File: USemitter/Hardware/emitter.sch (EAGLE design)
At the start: 8 parts, among them U5 LM1117MP-3.3

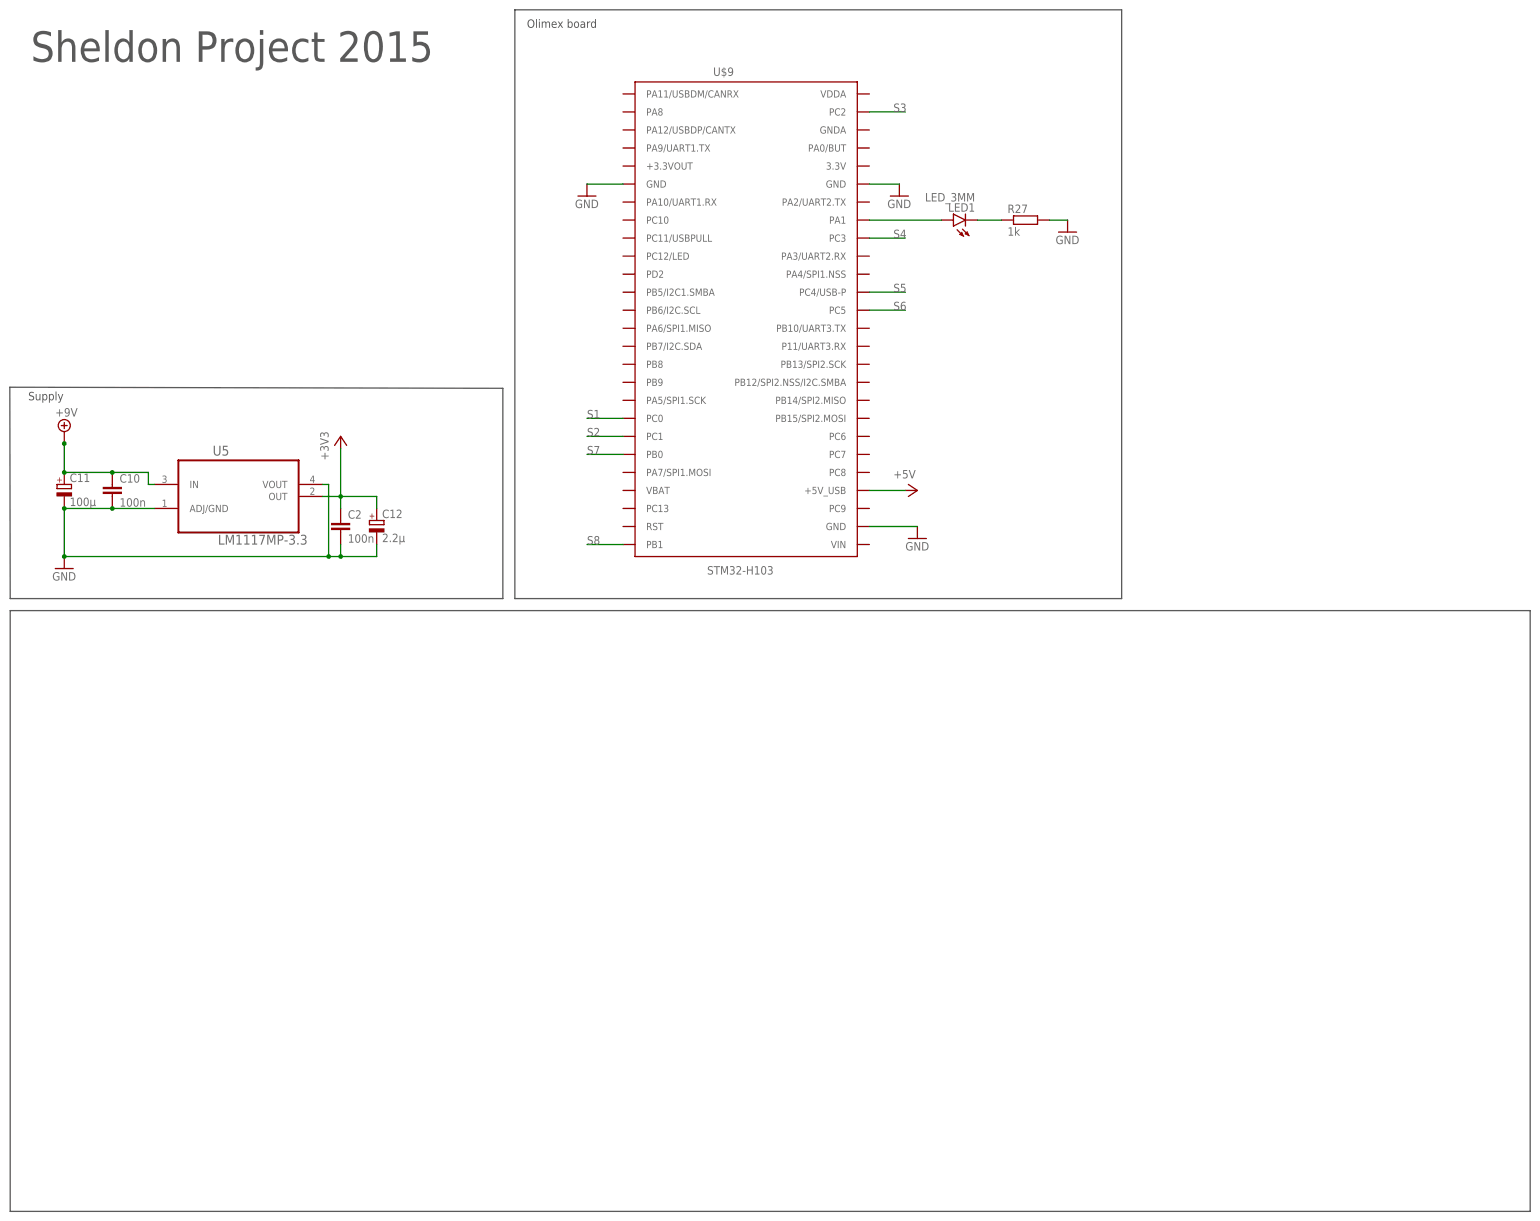
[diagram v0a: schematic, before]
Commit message: - Emitter schematic almost finished. - STM32 code generator modified to integrate the LED and the reversed PWM. ==> Code must still be generated
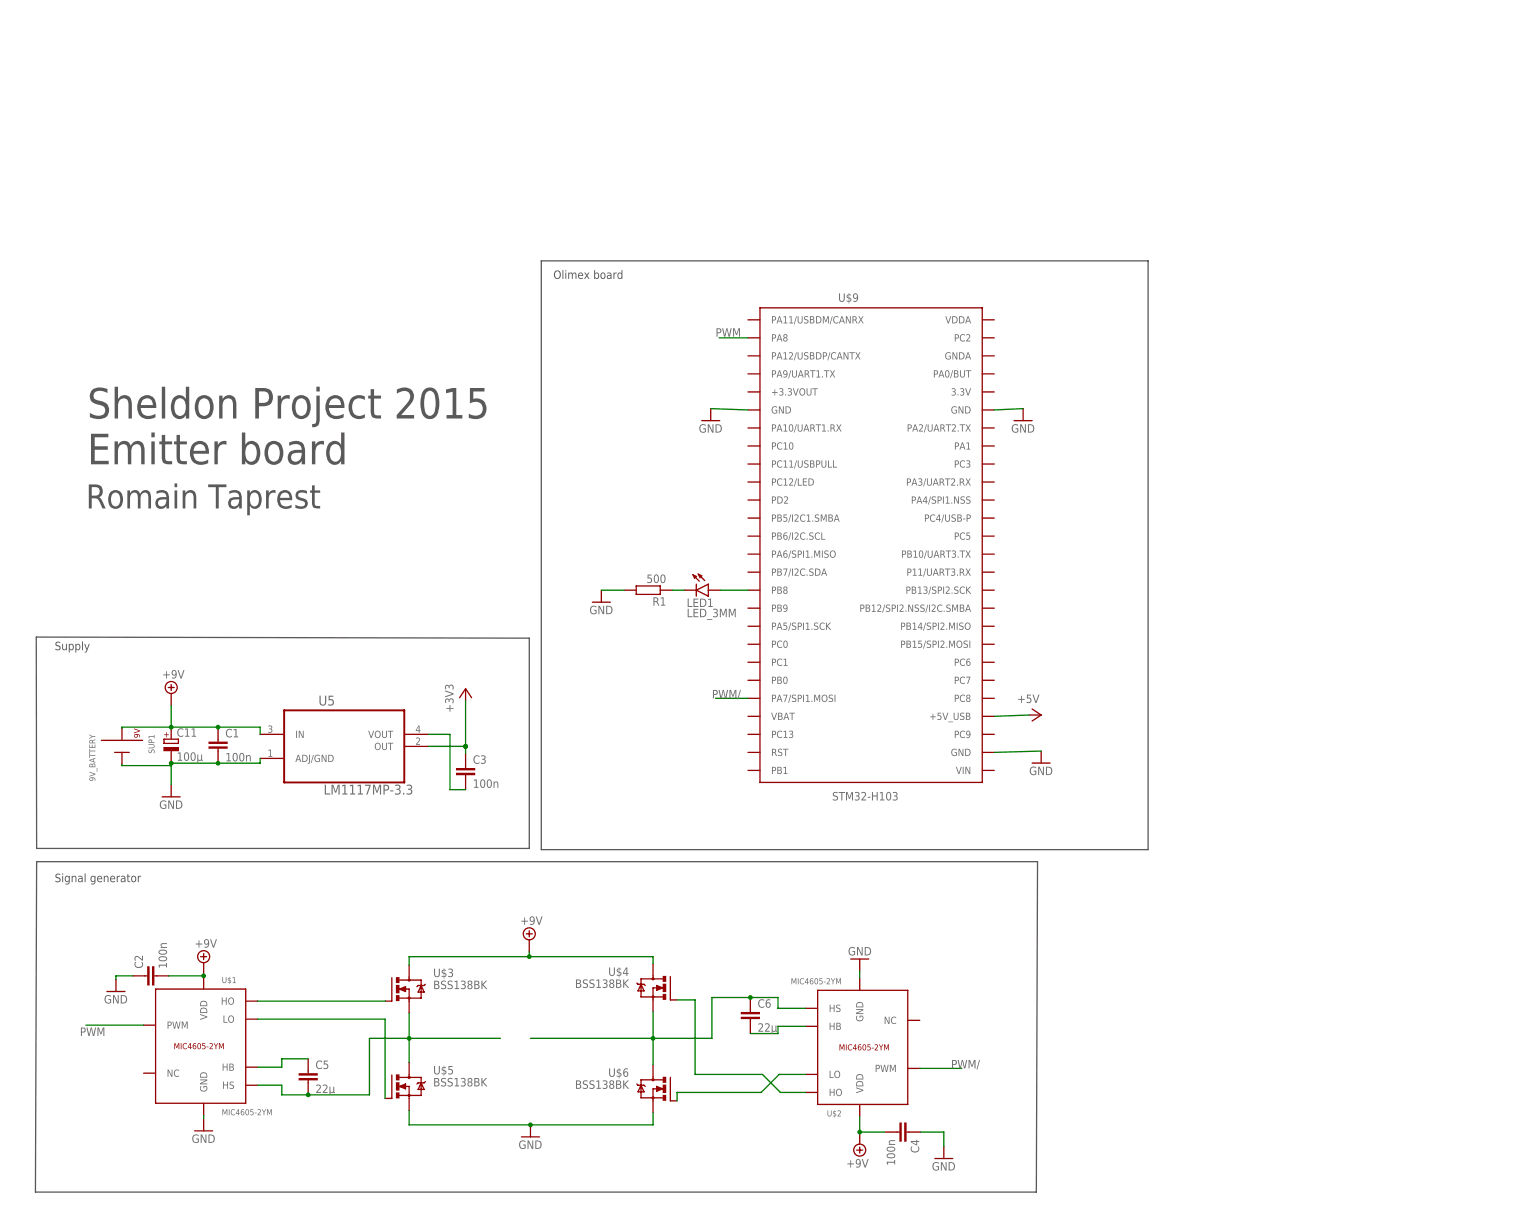
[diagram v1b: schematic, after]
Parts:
- removed C10: 100n, resistor:C-EUC0603
- removed C12: 2.2µ, @Club_passif:CPOL_DIAM5MM
- removed R27: 1k, resistor:R-EU_R0603
- added C1, C3, C4: 100n, resistor:C-EU050-025X075
- added C5, C6: 22µ, resistor:C-EU050-025X075
- added R1: 500, resistor:R-EU_0207/10
- added SUP1: 9V_BATTERY, libSheldonDrone:9V_BATTERY
- added U$1, U$2: MIC4605-2YM, libSheldonDrone:MIC4605-2YM
- added U$3, U$4, U$5, U$6: BSS138BK, libSheldonDrone:BSS138BK
- C2: device resistor:C-EUC0603 -> resistor:C-EU050-025X075
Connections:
- removed net N$17: LED1.A, U$9.PA1
- removed net N$18: LED1.C, R27.1
- removed net S1: U$9.PC0
- removed net S2: U$9.PC1
- removed net S3: U$9.PC2
- removed net S4: U$9.PC3
- removed net S5: U$9.PC4/USB-P
- removed net S6: U$9.PC5
- removed net S7: U$9.PB0
- removed net S8: U$9.PB1
- new net N$1: C3.2, U5.VOUT
- new net N$10: C6.1, U$2.HS, U$4.S, U$6.D
- new net N$11: U$2.HO, U$4.G
- new net N$13: LED1.A, U$9.PB8
- new net N$2: LED1.C, R1.1
- new net N$3: U$1.HO, U$3.G
- new net N$4: U$1.LO, U$5.G
- new net N$5: U$2.LO, U$6.G
- new net N$7: C5.1, U$1.HB
- new net N$8: C5.2, U$1.HS, U$3.S, U$5.D
- new net N$9: C6.2, U$2.HB
- new net PWM: U$1.PWM, U$9.PA8
- new net PWM/: U$2.PWM, U$9.PA7/SPI1.MOSI
- net +3V3: now also C3.1; no longer C12.P$1, C2.1
- net +9V: now also C1.1, C2.2, C4.2, SUP1.9V, U$1.VDD, U$2.VDD, U$3.D, U$4.D; no longer C10.1
- net GND: now also C1.2, C2.1, C4.1, R1.2, SUP1.GND, U$1.GND, U$2.GND, U$5.S, U$6.S; no longer C10.2, C12.P$2, C2.2, R27.2, U5.VOUT
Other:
- note added: "JACK"
- note added: "Romain Taprest"
- note added: "Sheldon Project 2015 Emitter board"
- note added: "Signal generator"
- note removed: "Sheldon Project 2015"
- moved on the sheet: C11, C2, LED1, U$9, U5

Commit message: Eagle files for the emitter board finished (designed and routed). To be verified and produce if OK.
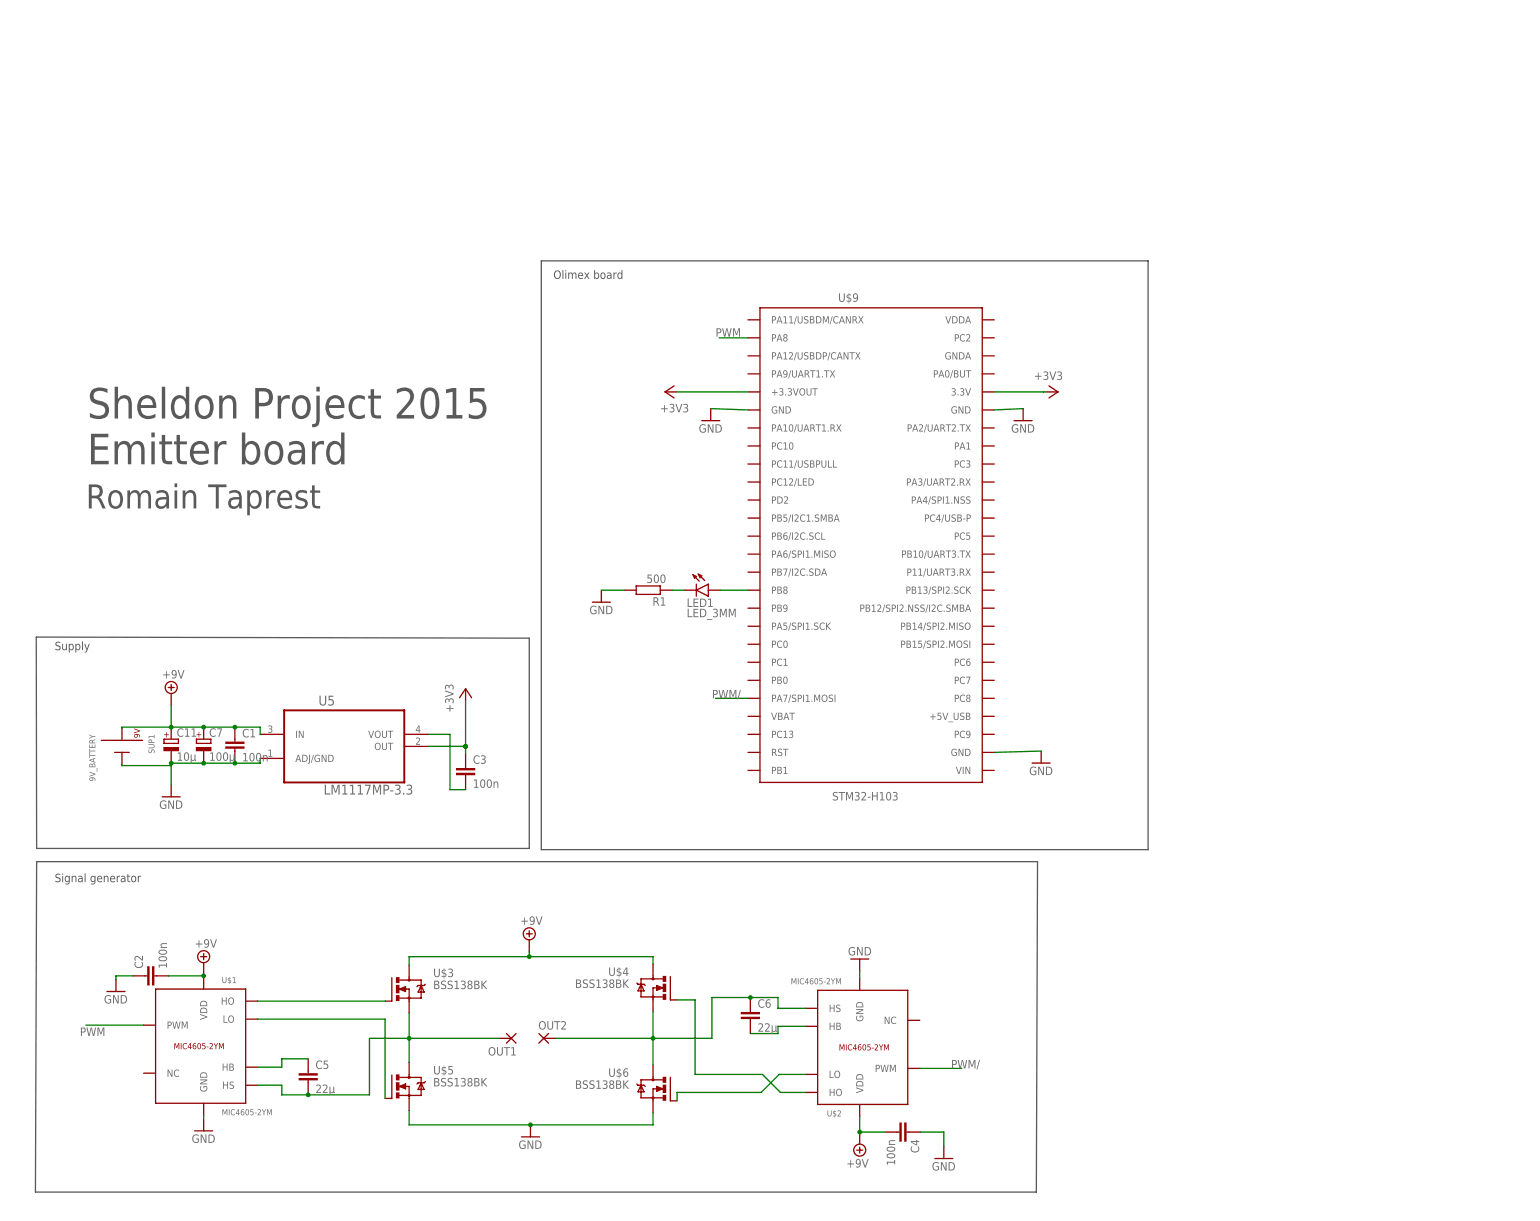
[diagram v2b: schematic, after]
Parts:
- added C7: 100µ, @Club_passif:CPOL_DIAM5MM
- added OUT1, OUT2: (no value), wirepad:2,54/1,0
- C11: value 100µ -> 10µ
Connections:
- removed net +5V: U$9.+5V_USB
- removed net N$10: C6.1, U$2.HS, U$4.S, U$6.D
- removed net N$8: C5.2, U$1.HS, U$3.S, U$5.D
- new net OUT1: C5.2, OUT1.P, U$1.HS, U$3.S, U$5.D
- new net OUT2: C6.1, OUT2.P, U$2.HS, U$4.S, U$6.D
- net +3V3: now also U$9.+3.3VOUT, U$9.3.3V
- net +9V: now also C7.P$1
- net GND: now also C7.P$2
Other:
- note removed: "JACK"
- moved on the sheet: C1
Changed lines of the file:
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@@
 <part name="+3V1" library="libSheldonDrone" deviceset="+3V3" device=""/>
 <part name="U5" library="libSheldonDrone" deviceset="LM1117MP-3.3" device=""/>
-<part name="C11" library="@Club_passif" deviceset="CPOL_" device="DIAM5MM" value="100µ"/>
+<part name="C11" library="@Club_passif" deviceset="CPOL_" device="DIAM5MM" value="10µ"/>
 <part name="U$9" library="libSheldonDrone" deviceset="STM32-H103" device=""/>
-<part name="P+11" library="libSheldonDrone" deviceset="+5V" device=""/>
 <part name="GND14" library="libSheldonDrone" deviceset="GND" device=""/>
 <part name="GND15" library="libSheldonDrone" deviceset="GND" device=""/>
@@
 <part name="SUPPLY4" library="supply2" deviceset="+9V" device=""/>
 <part name="SUP1" library="libSheldonDrone" deviceset="9V_BATTERY" device=""/>
+<part name="OUT2" library="wirepad" deviceset="2,54/1,0" device=""/>
+<part name="OUT1" library="wirepad" deviceset="2,54/1,0" device=""/>
+<part name="+3V2" library="libSheldonDrone" deviceset="+3V3" device=""/>
+<part name="+3V3" library="libSheldonDrone" deviceset="+3V3" device=""/>
+<part name="C7" library="@Club_passif" deviceset="CPOL_" device="DIAM5MM" value="100µ"/>
 </parts>
 <sheets>
@@
 <wire x1="117.348" y1="81.55" x2="117.348" y2="206.01" width="0.1524" layer="97"/>
 <text x="119.888" y="202.2" size="1.778" layer="97">Olimex board</text>
-<text x="109.474" y="43.688" size="1.778" layer="99" font="vector" ratio="13">JACK</text>
 <text x="14.478" y="74.676" size="1.778" layer="97" font="vector" ratio="13">Signal generator</text>
 <frame x1="0" y1="0.254" x2="255.778" y2="214.376" columns="8" rows="5" layer="94"/>
@@
 <instance part="C11" gate="G$1" x="39.116" y="104.902"/>
 <instance part="U$9" gate="G$1" x="161.036" y="193.548"/>
-<instance part="P+11" gate="1" x="223.012" y="110.0074" rot="R270"/>
 <instance part="GND14" gate="1" x="223.012" y="99.8474"/>
 <instance part="GND15" gate="1" x="153.162" y="172.2374"/>
@@
 <instance part="GND17" gate="1" x="130.048" y="133.858"/>
 <instance part="SUPPLY1" gate="G$1" x="39.116" y="114.554"/>
-<instance part="C1" gate="G$1" x="49.022" y="104.902"/>
+<instance part="C1" gate="G$1" x="52.578" y="104.902"/>
 <instance part="C3" gate="G$1" x="101.346" y="99.314"/>
 <instance part="R1" gate="G$1" x="139.954" y="136.398" rot="R180"/>
@@
 <instance part="SUPPLY4" gate="G$1" x="114.808" y="62.484"/>
 <instance part="SUP1" gate="G$1" x="28.702" y="107.188" rot="R270"/>
+<instance part="OUT2" gate="P" x="117.856" y="41.656"/>
+<instance part="OUT1" gate="P" x="110.998" y="41.656" rot="R180"/>
+<instance part="+3V2" gate="G$1" x="226.568" y="178.308" rot="R270"/>
+<instance part="+3V3" gate="G$1" x="143.51" y="178.308" rot="R90"/>
+<instance part="C7" gate="G$1" x="45.974" y="104.902"/>
 </instances>
 <busses>
@@
 <wire x1="39.116" y1="95.25" x2="39.116" y2="99.822" width="0.1524" layer="91"/>
 <pinref part="C1" gate="G$1" pin="2"/>
-<wire x1="39.116" y1="99.822" x2="49.022" y2="99.822" width="0.1524" layer="91"/>
+<wire x1="39.116" y1="99.822" x2="45.974" y2="99.822" width="0.1524" layer="91"/>
 <junction x="39.116" y="99.822"/>
 <pinref part="U5" gate="A" pin="ADJ/GND"/>
-<wire x1="49.022" y1="99.822" x2="57.912" y2="99.822" width="0.1524" layer="91"/>
+<wire x1="45.974" y1="99.822" x2="52.578" y2="99.822" width="0.1524" layer="91"/>
+<wire x1="52.578" y1="99.822" x2="57.912" y2="99.822" width="0.1524" layer="91"/>
 <wire x1="57.912" y1="99.822" x2="57.912" y2="100.838" width="0.1524" layer="91"/>
-<junction x="49.022" y="99.822"/>
+<junction x="52.578" y="99.822"/>
 <pinref part="SUP1" gate="G$1" pin="GND"/>
 <wire x1="28.702" y1="99.568" x2="28.702" y2="99.314" width="0.1524" layer="91"/>
 <wire x1="28.702" y1="99.314" x2="39.116" y2="99.314" width="0.1524" layer="91"/>
 <wire x1="39.116" y1="99.314" x2="39.116" y2="99.822" width="0.1524" layer="91"/>
+<pinref part="C7" gate="G$1" pin="P$2"/>
+<junction x="45.974" y="99.822"/>
 </segment>
 <segment>
@@
 </segment>
 </net>
-<net name="+5V" class="0">
-<segment>
-<pinref part="U$9" gate="G$1" pin="+5V_USB"/>
-<pinref part="P+11" gate="1" pin="+5V"/>
-<wire x1="213.106" y1="109.728" x2="220.472" y2="110.0074" width="0.1524" layer="91"/>
-</segment>
-</net>
 <net name="N$1" class="0">
 <segment>
@@
 <pinref part="C11" gate="G$1" pin="P$1"/>
 <pinref part="C1" gate="G$1" pin="1"/>
-<wire x1="39.116" y1="107.442" x2="49.022" y2="107.442" width="0.1524" layer="91"/>
+<wire x1="39.116" y1="107.442" x2="45.974" y2="107.442" width="0.1524" layer="91"/>
 <pinref part="U5" gate="A" pin="IN"/>
-<wire x1="49.022" y1="107.442" x2="57.912" y2="107.442" width="0.1524" layer="91"/>
+<wire x1="45.974" y1="107.442" x2="52.578" y2="107.442" width="0.1524" layer="91"/>
+<wire x1="52.578" y1="107.442" x2="57.912" y2="107.442" width="0.1524" layer="91"/>
 <wire x1="57.912" y1="107.442" x2="57.912" y2="105.918" width="0.1524" layer="91"/>
-<junction x="49.022" y="107.442"/>
+<junction x="52.578" y="107.442"/>
 <pinref part="SUPPLY1" gate="G$1" pin="+9V"/>
 <wire x1="39.116" y1="112.014" x2="39.116" y2="107.442" width="0.1524" layer="91"/>
@@
 <wire x1="28.702" y1="107.188" x2="28.702" y2="107.442" width="0.1524" layer="91"/>
 <wire x1="28.702" y1="107.442" x2="39.116" y2="107.442" width="0.1524" layer="91"/>
+<pinref part="C7" gate="G$1" pin="P$1"/>
+<junction x="45.974" y="107.442"/>
 </segment>
 <segment>
@@
 <junction x="101.346" y="103.378"/>
 </segment>
+<segment>
+<pinref part="U$9" gate="G$1" pin="3.3V"/>
+<pinref part="+3V2" gate="G$1" pin="+3V3"/>
+<wire x1="213.106" y1="178.308" x2="223.52" y2="178.308" width="0.1524" layer="91"/>
+<wire x1="223.52" y1="178.308" x2="224.028" y2="178.308" width="0.1524" layer="91"/>
+</segment>
+<segment>
+<pinref part="+3V3" gate="G$1" pin="+3V3"/>
+<pinref part="U$9" gate="G$1" pin="+3.3VOUT"/>
+<wire x1="146.05" y1="178.308" x2="161.036" y2="178.308" width="0.1524" layer="91"/>
+</segment>
 </net>
 <net name="N$2" class="0">
@@
 </segment>
 </net>
-<net name="N$8" class="0">
+<net name="OUT1" class="0">
 <segment>
 <pinref part="U$1" gate="G$1" pin="HS"/>
@@
 <wire x1="81.026" y1="41.656" x2="89.408" y2="41.656" width="0.1524" layer="91"/>
 <junction x="89.408" y="41.656"/>
-<wire x1="89.408" y1="41.656" x2="108.712" y2="41.656" width="0.1524" layer="91"/>
+<wire x1="89.408" y1="41.656" x2="108.458" y2="41.656" width="0.1524" layer="91"/>
+<pinref part="OUT1" gate="P" pin="P"/>
 </segment>
 </net>
@@
 </segment>
 </net>
-<net name="N$10" class="0">
+<net name="OUT2" class="0">
 <segment>
 <pinref part="U$2" gate="G$1" pin="HS"/>
@@
 <wire x1="140.97" y1="41.656" x2="140.97" y2="36.068" width="0.1524" layer="91"/>
 <junction x="140.97" y="41.656"/>
-<wire x1="140.97" y1="41.656" x2="115.062" y2="41.656" width="0.1524" layer="91"/>
-</segment>
-</net>
+<wire x1="140.97" y1="41.656" x2="120.396" y2="41.656" width="0.1524" layer="91"/>
+<pinref part="OUT2" gate="P" pin="P"/>
+</segment>
+</net>

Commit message: Final version of the emitter board
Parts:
- U$1, U$2: value MIC4605-2YM -> MIC4605-1YM; device libSheldonDrone:MIC4605-2YM -> libSheldonDrone:MIC4605-1YM
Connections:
- net +9V: now also U$2.GND; no longer U$2.VDD
- net GND: now also U$2.VDD; no longer U$2.GND
- net N$9: now also U$2.HS; no longer U$2.HB
- net OUT2: now also U$2.HB; no longer U$2.HS
- net PWM: now also U$1.HI, U$2.LI; no longer U$1.PWM
- net PWM/: now also U$1.LI, U$2.HI; no longer U$2.PWM
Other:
- moved on the sheet: C6, U$2
